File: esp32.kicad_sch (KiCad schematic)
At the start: 25 parts, among them J2 TC2030-IDC, J3 Conn_01x04, J4 Conn_01x06, J5 USB_C_Receptacle_USB2.0, SW1 GT-TC029B-H025-L1N, SW2 GT-TC029B-H025-L1N, U23 LM358, U3 RT9080-33GJ5, U4 ESP32-S3-WROOM-1

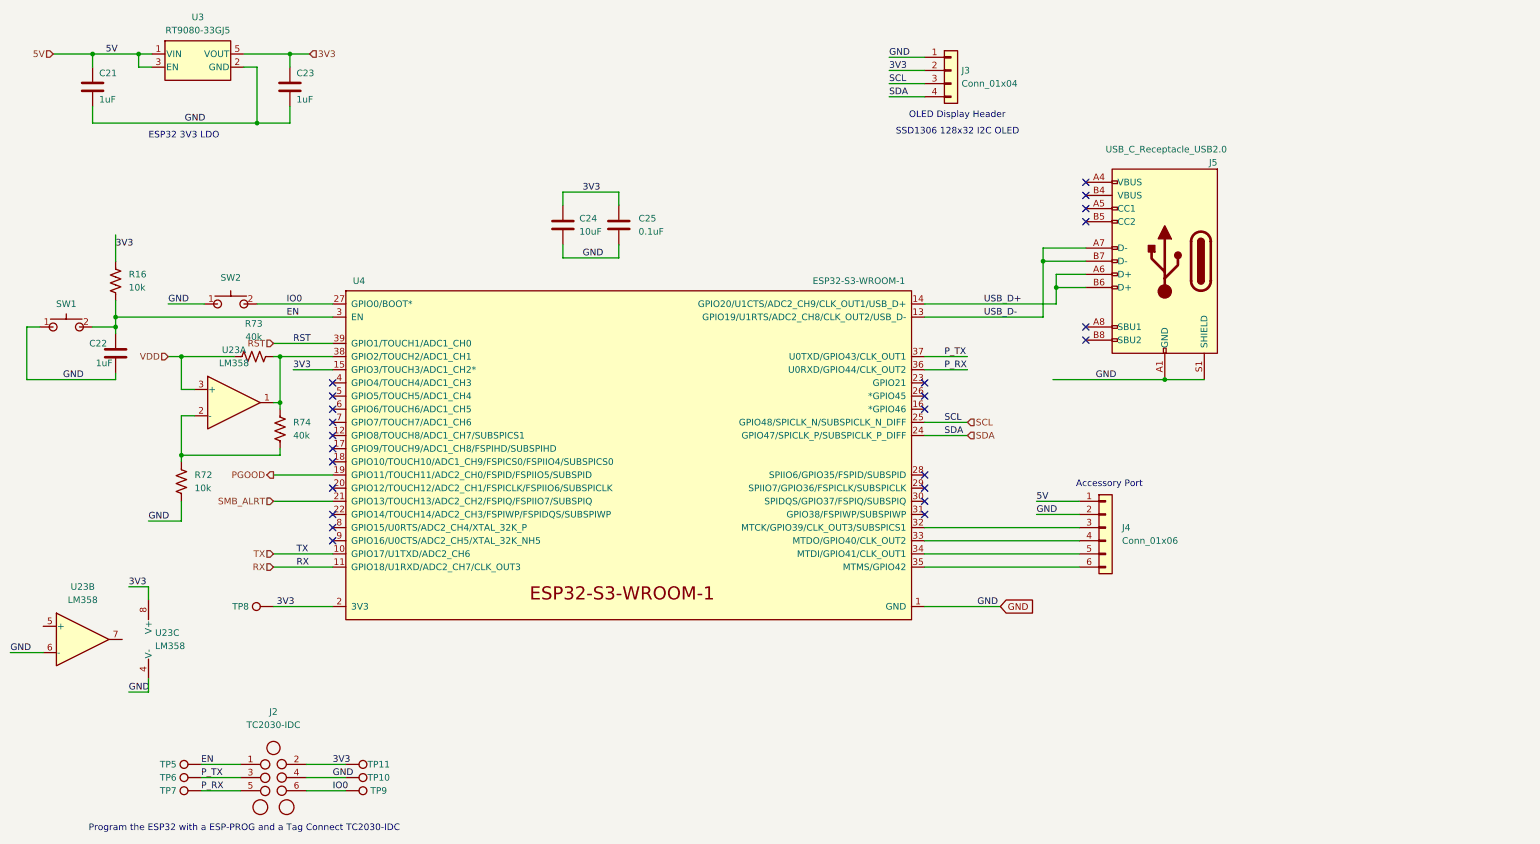
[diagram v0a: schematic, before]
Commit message: All components placed
Went through TI schematic and layout checklist.
All components placed and initial DRC
Need thermal vias on KF1950 and also better layout (so not so many errors)
Need to do silk
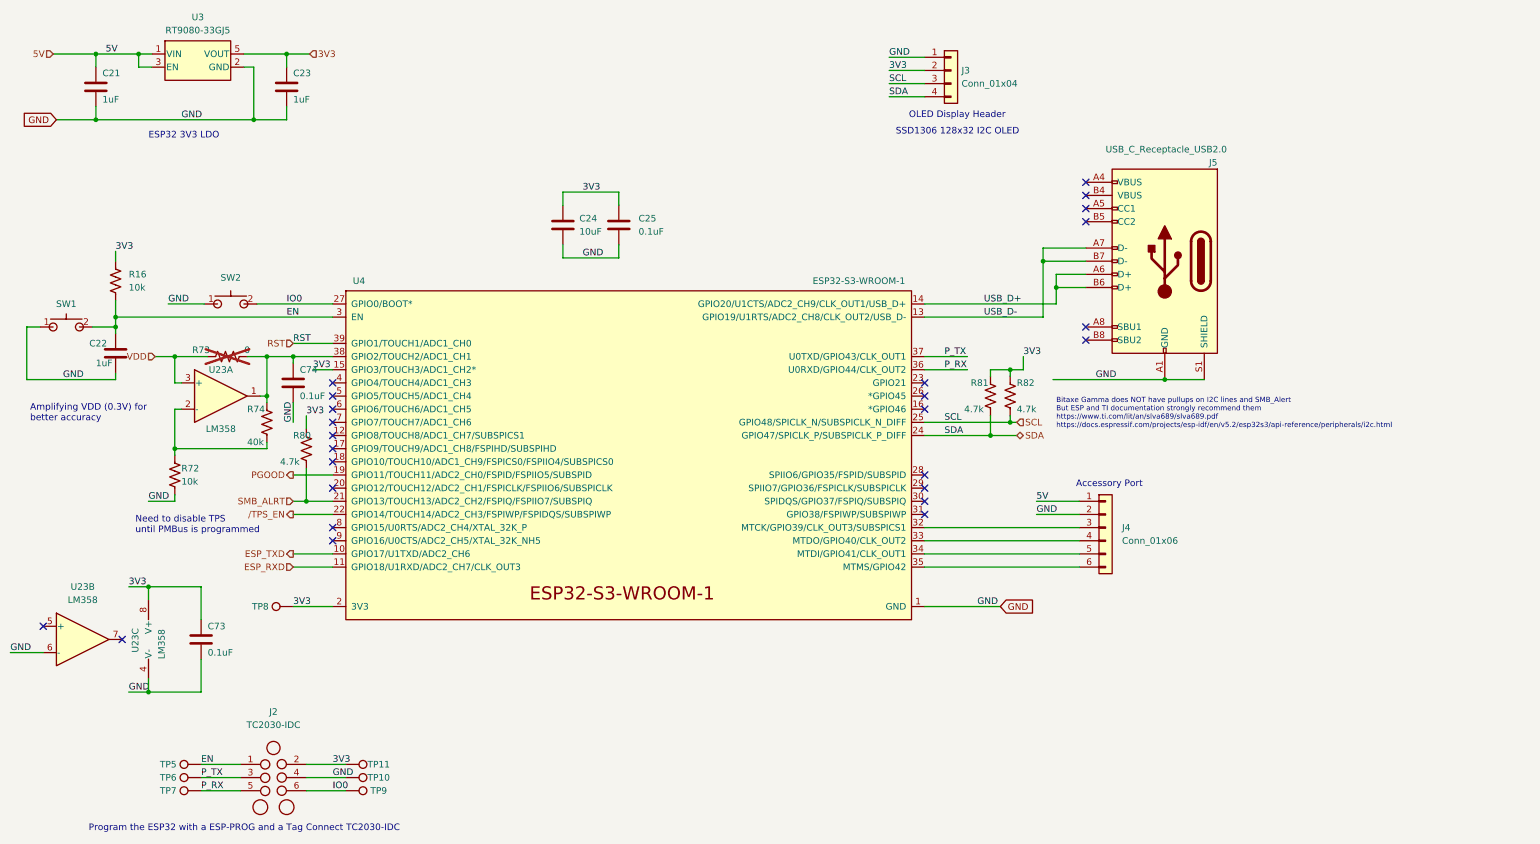
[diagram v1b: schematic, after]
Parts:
- added C73, C74: 0.1uF, Capacitor_SMD:C_0402_1005Metric, symbol Device:C
- added R80, R81, R82: 4.7k, Resistor_SMD:R_0402_1005Metric, symbol Device:R_US
- R73: value 40k -> 0; now not fitted
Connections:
- net 3V3: now also C73.1, R80.1, R81.1, R82.1
- net GND: now also C73.2, C74.2
- net SCL: now also R82.2
- net SDA: now also R81.2
- net SMB_ALRT: now also R80.2
- net at R73.2, R74.1, U23.1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: now also C74.1
- net /TPS_EN: now reaches U4.22 (GPIO14/TOUCH14/ADC2_CH3/FSPIWP/FSPIDQS/SUBSPIWP)
- net RX renamed ESP_RXD
- net TX renamed ESP_TXD
- no-connect marks 24 -> 25
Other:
- note added: "Amplifying VDD (0.3V) for better accuracy"
- note added: "Bitaxe Gamma does NOT have pullups on I2C lines and SMB_Alert But ESP and TI documentation strongly recommend them https://www.ti.com/lit/an/slva689/slva689.pdf https://docs.espressif.com/projects/esp-idf/en/v5.2/esp32s3/api-reference/peripherals/i2c.html"
- note added: "Need to disable TPS until PMBus is programmed"
- moved on the sheet: C21, C23, R72, R74, TP8, U23A

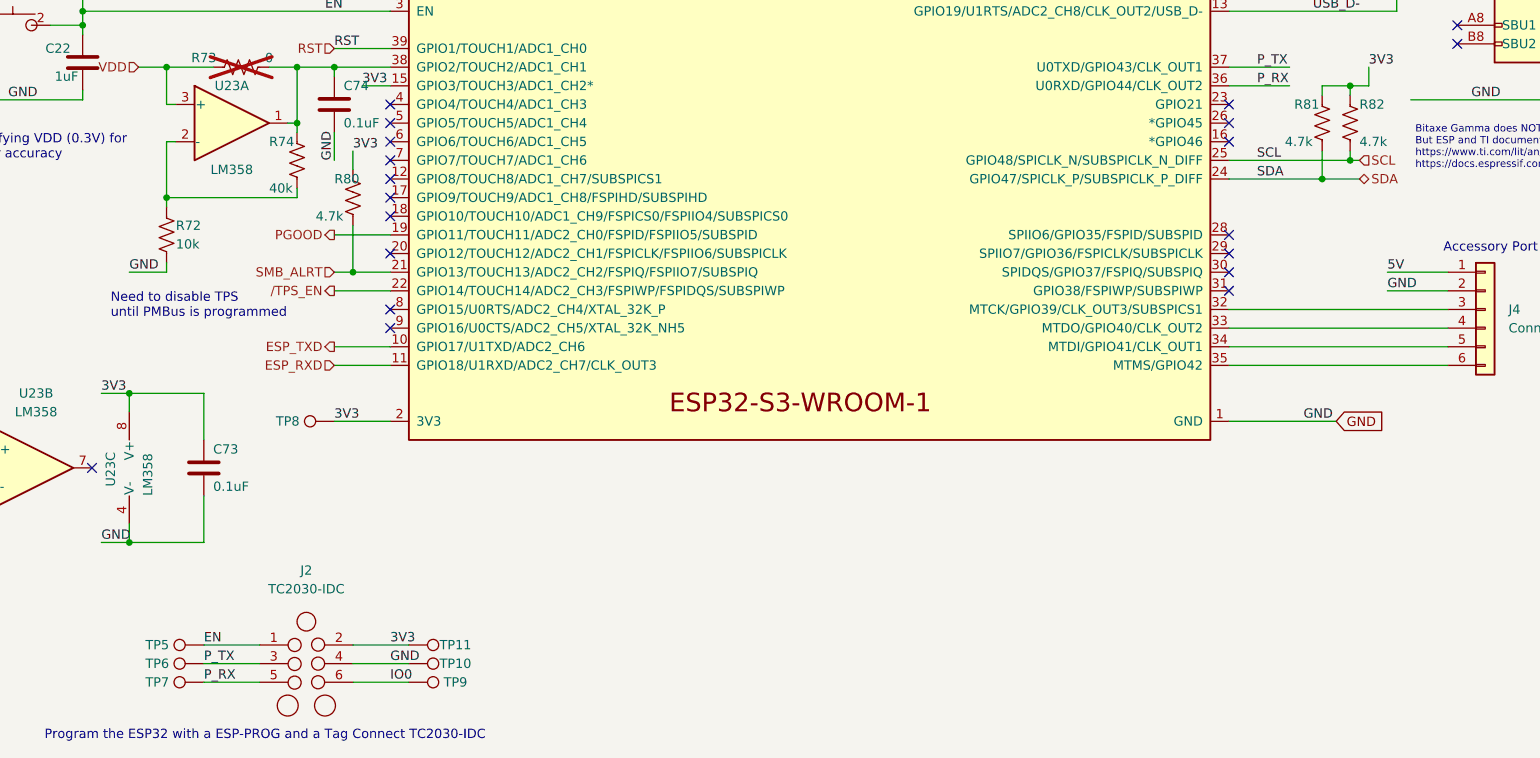
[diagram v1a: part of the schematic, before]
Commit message: Manfacturing prep
Add part numbers and did initial BOM optimization (Hope to do more after testing)
Created Manufacturing files
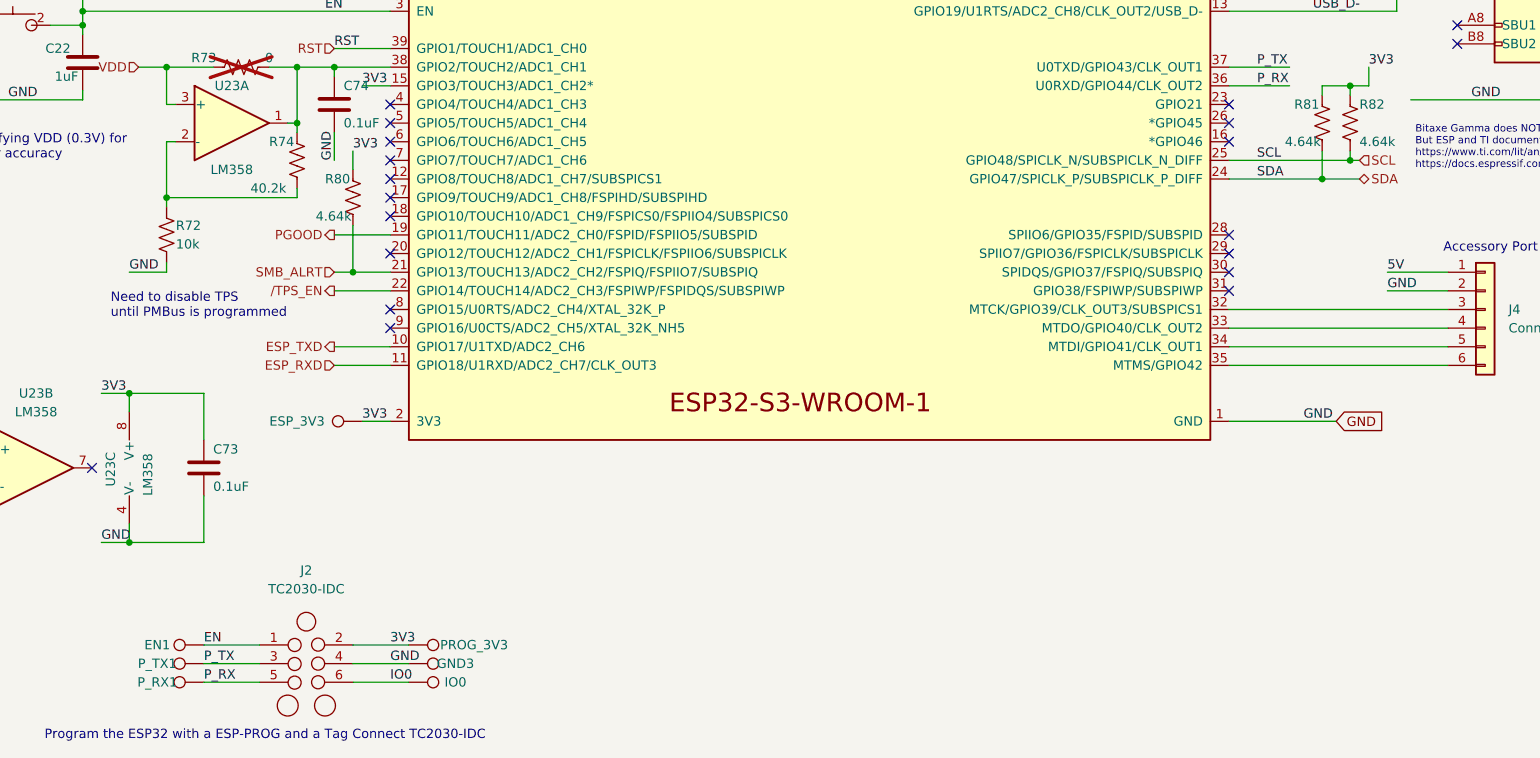
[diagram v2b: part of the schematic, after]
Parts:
- R74: value 40k -> 40.2k
- R80, R81, R82: value 4.7k -> 4.64k
- renumbered TP5 to EN1, TP8 to ESP_3V3, TP10 to GND3, TP9 to IO0, TP11 to PROG_3V3, TP7 to P_RX1, TP6 to P_TX1
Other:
- moved on the sheet: ESP_3V3
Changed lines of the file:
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@@
 	(wire
 		(pts
+			(xy 73.66 135.89) (xy 77.47 135.89)
+		)
+		(stroke
+			(width 0)
+			(type default)
+		)
+	)
+	(wire
+		(pts
 			(xy 35.56 80.01) (xy 77.47 80.01)
 		)
@@
 	(wire
 		(pts
-			(xy 69.85 135.89) (xy 77.47 135.89)
-		)
-		(stroke
-			(width 0)
-			(type default)
-		)
-	)
-	(wire
-		(pts
 			(xy 184.912 37.465) (xy 191.77 37.465)
 		)
@@
 	)
 	(label "3V3"
-		(at 69.85 135.89 0)
+		(at 73.66 135.89 0)
 		(effects
 			(font
@@
 			)
 		)
-		(property "Value" "40k"
-			(at 60.96 104.14 0)
+		(property "Value" "40.2k"
+			(at 58.42 104.14 0)
 			(effects
 				(font
@@
 		(on_board yes)
 		(dnp no)
-		(property "Reference" "TP6"
+		(property "Reference" "P_TX1"
 			(at 45.72 168.91 90)
 			(effects
@@
 			(project "bitaxeGamma"
 				(path "/e63e39d7-6ac0-4ffd-8aa3-1841a4541b55/ca857324-2ec8-447e-bd58-90d0c2e6b6d7"
-					(reference "TP6")
+					(reference "P_TX1")
 					(unit 1)
 				)
@@
 		(on_board yes)
 		(dnp no)
-		(property "Reference" "TP9"
+		(property "Reference" "IO0"
 			(at 86.36 171.45 90)
 			(effects
@@
 			(project "bitaxeGamma"
 				(path "/e63e39d7-6ac0-4ffd-8aa3-1841a4541b55/ca857324-2ec8-447e-bd58-90d0c2e6b6d7"
-					(reference "TP9")
+					(reference "IO0")
 					(unit 1)
 				)
@@
 		(on_board yes)
 		(dnp no)
-		(property "Reference" "TP11"
-			(at 86.36 166.37 90)
+		(property "Reference" "PROG_3V3"
+			(at 88.9 166.37 90)
 			(effects
 				(font
@@
 			(project "bitaxeGamma"
 				(path "/e63e39d7-6ac0-4ffd-8aa3-1841a4541b55/ca857324-2ec8-447e-bd58-90d0c2e6b6d7"
-					(reference "TP11")
+					(reference "PROG_3V3")
 					(unit 1)
 				)
@@
 		(on_board yes)
 		(dnp no)
-		(property "Reference" "TP10"
+		(property "Reference" "GND3"
 			(at 86.36 168.91 90)
 			(effects
@@
 			(project "bitaxeGamma"
 				(path "/e63e39d7-6ac0-4ffd-8aa3-1841a4541b55/ca857324-2ec8-447e-bd58-90d0c2e6b6d7"
-					(reference "TP10")
+					(reference "GND3")
 					(unit 1)
 				)
@@
 		(dnp no)
 		(property "Reference" "R80"
-			(at 69.85 102.87 0)
+			(at 68.58 102.87 0)
 			(effects
 				(font
@@
 			)
 		)
-		(property "Value" "4.7k"
+		(property "Value" "4.64k"
 			(at 67.31 107.95 0)
 			(effects
@@
 	(symbol
 		(lib_id "Connector:TestPoint")
-		(at 69.85 135.89 90)
+		(at 73.66 135.89 90)
 		(mirror x)
 		(unit 1)
@@
 		(on_board yes)
 		(dnp no)
-		(property "Reference" "TP8"
-			(at 63.5 135.89 90)
+		(property "Reference" "ESP_3V3"
+			(at 64.77 135.89 90)
 			(effects
 				(font
@@
 		)
 		(property "Value" "TestPoint"
-			(at 64.135 137.1599 90)
+			(at 67.945 137.1599 90)
 			(effects
 				(font
@@
 		)
 		(property "Footprint" "TestPoint:TestPoint_Pad_D1.5mm"
-			(at 69.85 140.97 0)
+			(at 73.66 140.97 0)
 			(effects
 				(font
@@
 		)
 		(property "Datasheet" "~"
-			(at 69.85 140.97 0)
+			(at 73.66 140.97 0)
 			(effects
 				(font
@@
 		)
 		(property "Description" "test point"
-			(at 69.85 135.89 0)
+			(at 73.66 135.89 0)
 			(effects
 				(font
@@
 			(project "bitaxeGamma"
 				(path "/e63e39d7-6ac0-4ffd-8aa3-1841a4541b55/ca857324-2ec8-447e-bd58-90d0c2e6b6d7"
-					(reference "TP8")
+					(reference "ESP_3V3")
 					(unit 1)
 				)
@@
 		(on_board yes)
 		(dnp no)
-		(property "Reference" "TP5"
+		(property "Reference" "EN1"
 			(at 45.72 166.37 90)
 			(effects
@@
 			(project "bitaxeGamma"
 				(path "/e63e39d7-6ac0-4ffd-8aa3-1841a4541b55/ca857324-2ec8-447e-bd58-90d0c2e6b6d7"
-					(reference "TP5")
+					(reference "EN1")
 					(unit 1)
 				)
@@
 			)
 		)
-		(property "Value" "4.7k"
+		(property "Value" "4.64k"
 			(at 199.39 97.79 0)
 			(effects
@@
 		(on_board yes)
 		(dnp no)
-		(property "Reference" "TP7"
+		(property "Reference" "P_RX1"
 			(at 45.72 171.45 90)
 			(effects
@@
 			(project "bitaxeGamma"
 				(path "/e63e39d7-6ac0-4ffd-8aa3-1841a4541b55/ca857324-2ec8-447e-bd58-90d0c2e6b6d7"
-					(reference "TP7")
+					(reference "P_RX1")
 					(unit 1)
 				)
@@
 			)
 		)
-		(property "Value" "4.7k"
+		(property "Value" "4.64k"
 			(at 209.55 97.79 0)
 			(effects

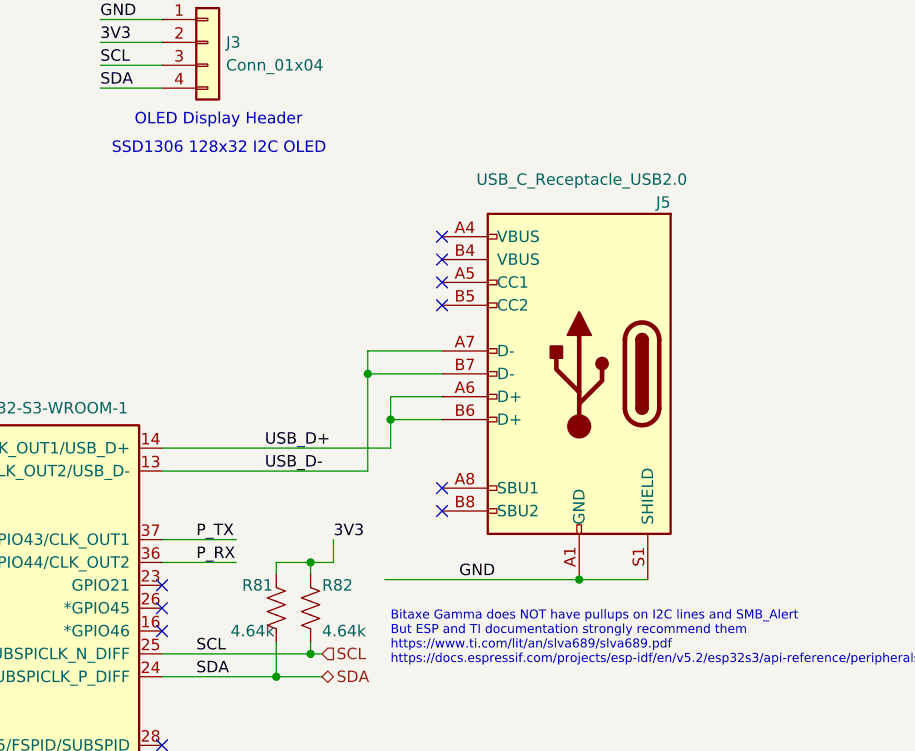
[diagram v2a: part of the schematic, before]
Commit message: Addressed Bitaxe Gamma Issues
- moved Fan caps
- added USB CC1 & CC2 pulldowns
- (I2C pullups were already done)
- reviewed but so far did not address any of the other issues/bugs
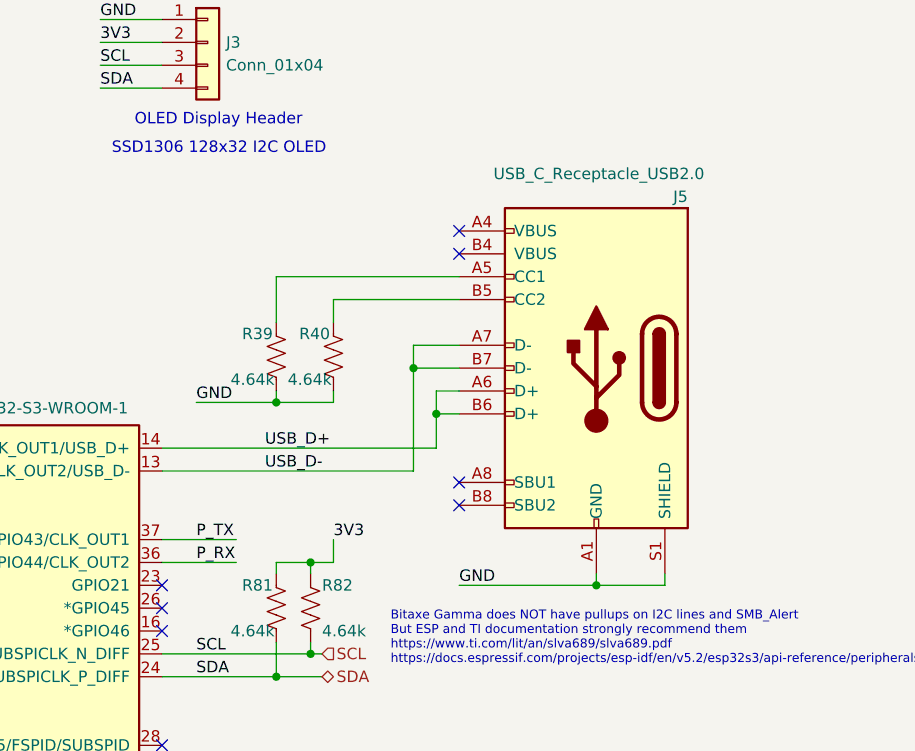
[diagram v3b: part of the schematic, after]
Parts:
- added R39, R40: 4.64k, Resistor_SMD:R_0402_1005Metric, symbol Device:R_US
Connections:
- net GND: now also R39.2, R40.2
- net at J5.A5 (CC1): now also R39.1
- net at J5.B5 (CC2): now also R40.1
- no-connect marks 25 -> 23
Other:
- moved on the sheet: J5
